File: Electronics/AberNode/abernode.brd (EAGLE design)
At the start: 100 x 80 mm, 12 parts, among them IC1 MCP1703CB, Y1 16MHZ, Y2 16MHZ

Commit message: Schematic Mostly Done
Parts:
- removed Y1: 16MHZ, SparkFun-FreqCtrl:RESONATOR-SMD
- added BATT, SOLAR: M02LOCK, SparkFun-Connectors:1X02_LOCK
- added C6, C9: 10uF, resistor:C0805
- added C7: (no value), resistor:E7,5-18
- added CHRG/LBO: ORANGE, led:CHIPLED_0603
- added CON4: (no value), SparkFun-Connectors:1X06_LONGPADS
- added D1: MBR0520LT, diode:SOD123
- added DONE: GREEN, led:CHIPLED_0603
- added IC2: MCP73871, adafruit:QFN20
- added PWR: RED, led:CHIPLED_0603
- added R2, R3, R9: 10k, resistor:R0805
- added R4: 2K, resistor:R0805
- added R5: 100K, resistor:R0805
- added R6, R7, R8: 1K, resistor:R0805
- added U$1: (no value), tom:ANT
- added U$2, U$3, U$4: HEADER_4, tom:HEADER_4
- moved R1 96.7 mm to (35.8, 40.8), turned to 90 degrees
- moved C5 94.8 mm to (32.3, 36.3)
- moved Y2 89.4 mm to (31.5, 43.9), turned to 90 degrees
- moved FLASH 82.5 mm to (36.0, 57.7)
- moved C4 74.9 mm to (11.0, 41.4), turned to 180 degrees
- moved C2 71.6 mm to (27.3, 29.5)
- moved C1 70.8 mm to (31.8, 24.5)
- moved RFM 63.7 mm to (22.0, 52.8), flipped to the bottom, turned to 90 degrees
- moved C3 63.0 mm to (32.0, 27.1)
- moved IC1 56.2 mm to (31.8, 30.5), turned to 270 degrees
- moved ATMEGA 50.3 mm to (21.9, 42.2), turned to 180 degrees
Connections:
- removed net PSBATT: C1.2, C3.2, IC1.3
- removed net VCC: C2.2, IC1.2
- new net ANALOG_1: ATMEGA.37, U$2.4
- new net ANALOG_2: ATMEGA.36, U$3.4
- new net ANALOG_3: ATMEGA.35, U$4.4
- new net ANALOG_4: ATMEGA.34, CON4.6
- new net DIGIT_1: ATMEGA.9, U$2.3
- new net DIGIT_2: ATMEGA.10, U$3.3
- new net DIGIT_3: ATMEGA.11, U$4.3
- new net N$10: CHRG/LBO.A, R8.1
- new net N$11: IC2.6, PWR.C
- new net N$12: DONE.C, IC2.7
- new net N$13: CHRG/LBO.C, IC2.8
- new net N$14: D1.A, SOLAR.2
- new net N$17: IC2.5, R9.2
- new net N$5: IC2.12, R5.2
- new net N$6: IC2.2, R2.2, R3.1
- new net N$7: IC2.13, R4.2
- new net N$8: PWR.A, R6.1
- new net N$9: DONE.A, R7.1
- new net SCL: ATMEGA.19, CON4.5
- new net SDA: ATMEGA.20, CON4.4
- new net VBATT: BATT.2, C6.2, IC2.14, IC2.15, IC2.16
- new net VIN: C7.+, C9.2, CON4.2, D1.C, IC2.17, IC2.18, IC2.19, IC2.3, IC2.4, IC2.9, R3.2, R6.2, R7.2, R8.2
- new net VSUPPLY: C1.2, C3.2, IC1.3, IC2.1, IC2.20
- net +3V3: now also C2.2, CON4.1, IC1.2, U$2.2, U$3.2, U$4.2
- net ANT: now also U$1.P$1
- net GND: now also BATT.1, C6.1, C7.-, C9.1, CON4.3, IC2.10, IC2.11, R2.1, R4.1, R5.1, R9.1, SOLAR.1, U$2.1, U$3.1, U$4.1
- net N$3: now also ATMEGA.29
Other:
- board size 100 x 80 mm -> 40.6 x 65.9 mm

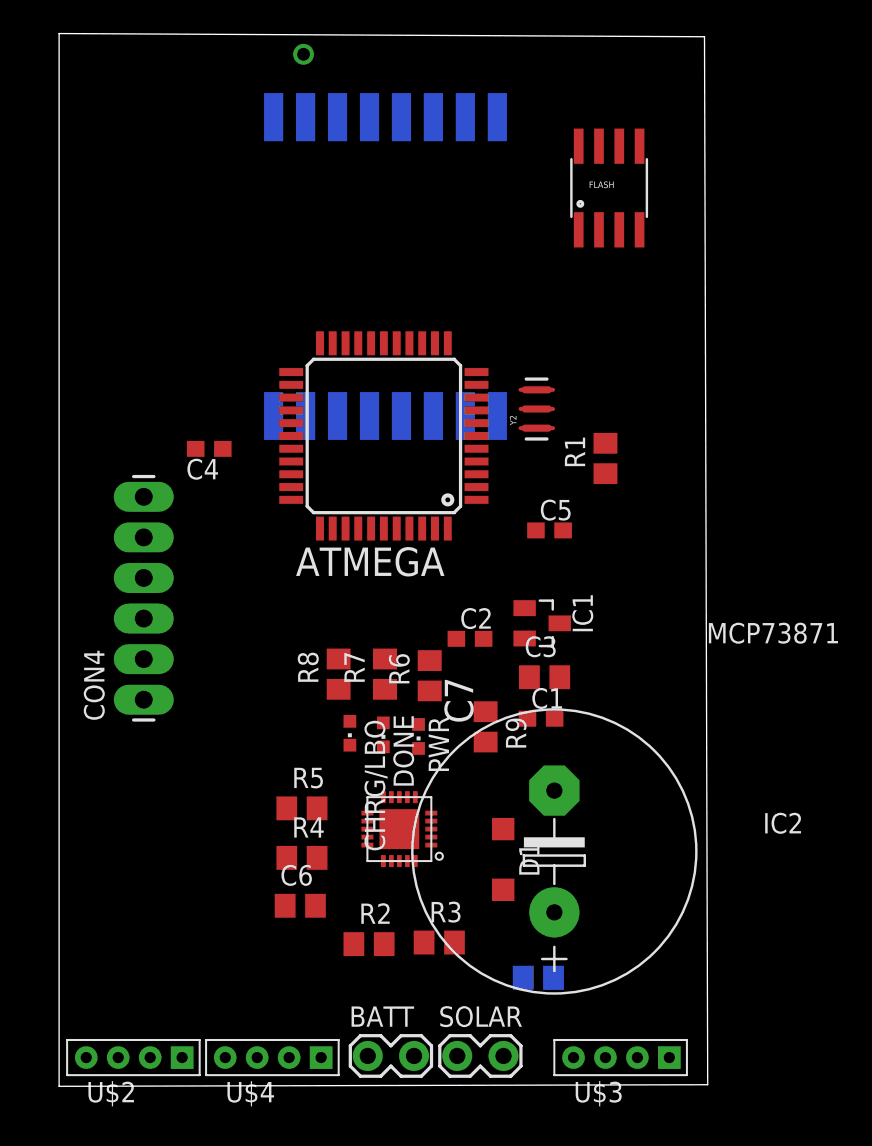
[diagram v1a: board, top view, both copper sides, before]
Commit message: Board Designed minus res values
Need to sort out the resistor values for the mcp73871 pullups battery
sense and charging rates.
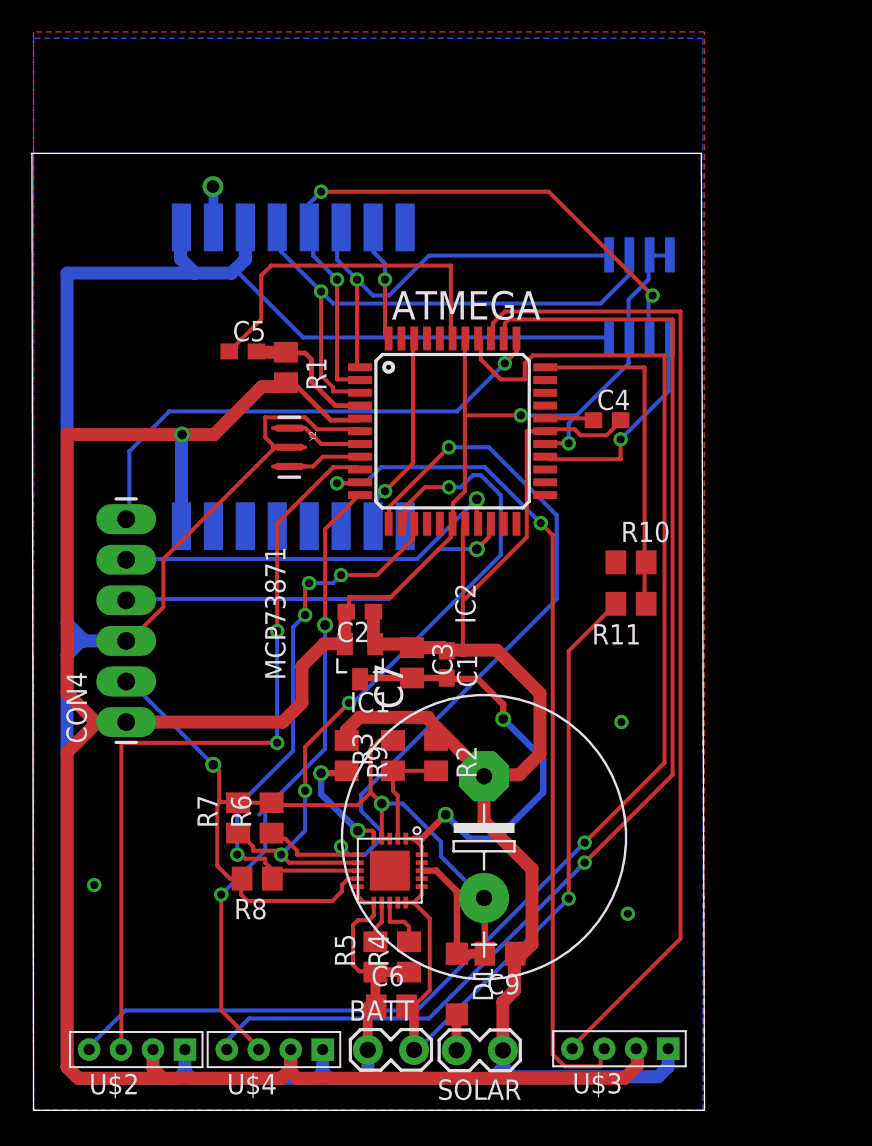
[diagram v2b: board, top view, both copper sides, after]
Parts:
- removed CHRG/LBO: ORANGE, led:CHIPLED_0603
- removed DONE: GREEN, led:CHIPLED_0603
- removed PWR: RED, led:CHIPLED_0603
- added R10, R11: 10k, resistor:R0805
- moved C4 25.0 mm to (35.9, 43.2), turned to 0 degrees
- moved C5 22.2 mm to (13.1, 47.5)
- moved R1 20.8 mm to (15.8, 46.5), turned to 270 degrees
- moved Y2 15.7 mm to (16.0, 41.5), turned to 270 degrees
- moved R8 13.8 mm to (14.0, 14.5), turned to 180 degrees
- moved R6 13.3 mm to (14.9, 18.3)
- moved R7 12.9 mm to (12.8, 18.3)
- moved R2 12.5 mm to (25.2, 22.2), turned to 270 degrees
- moved R3 12.1 mm to (22.5, 22.2), turned to 90 degrees
- moved IC1 11.6 mm to (20.4, 28.1), turned to 180 degrees
- moved R5 10.4 mm to (21.4, 9.60), turned to 90 degrees
- moved U$1 10.0 mm to (11.2, 57.8), flipped to the bottom
- moved R4 9.13 mm to (23.5, 9.60), turned to 90 degrees
- moved RFM 8.99 mm to (16.3, 45.9)
- moved R9 8.88 mm to (19.6, 22.2)
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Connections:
- removed net N$10: CHRG/LBO.A, R8.1
- removed net N$11: IC2.6, PWR.C
- removed net N$12: DONE.C, IC2.7
- removed net N$13: CHRG/LBO.C, IC2.8
- removed net N$8: PWR.A, R6.1
- removed net N$9: DONE.A, R7.1
- new net BATT_SENSE: ATMEGA.33, R10.2, R11.1
- new net PG: ATMEGA.12, IC2.6, R6.1
- new net STAT1: ATMEGA.14, IC2.8, R8.1
- new net STAT2: ATMEGA.13, IC2.7, R7.1
- net GND: now also R10.1
- net VBATT: now also R11.2
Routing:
- net GND: track 0.00 -> 294.8 mm, vias 0 -> 3
- net +3V3: track 0.00 -> 176.8 mm, vias 0 -> 3
- net ANALOG_1: track 0.00 -> 83.7 mm, vias 0 -> 1
- net ANALOG_3: track 0.00 -> 75.4 mm, vias 0 -> 1
- net VIN: track 0.00 -> 65.9 mm, vias 0 -> 2
- net ANALOG_2: track 0.00 -> 62.0 mm
- net DIGIT_2: track 0.00 -> 54.2 mm, vias 0 -> 2
- net PG: track 0.00 -> 50.6 mm, vias 0 -> 2
- net DIGIT_1: track 0.00 -> 49.4 mm, vias 0 -> 2
- net VBATT: track 0.00 -> 46.5 mm, vias 0 -> 1
- net STAT2: track 0.00 -> 45.3 mm, vias 0 -> 4
- net MISO: track 0.00 -> 40.6 mm, vias 0 -> 3
- net DIGIT_3: track 0.00 -> 39.9 mm, vias 0 -> 2
- net STAT1: track 0.00 -> 36.6 mm, vias 0 -> 4
- net SCK: track 0.00 -> 35.1 mm, vias 0 -> 1
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- added copper zone on layer 1, net GND
- added copper zone on layer 16, net GND
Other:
- board size 40.6 x 65.9 mm -> 42.1 x 59.9 mm

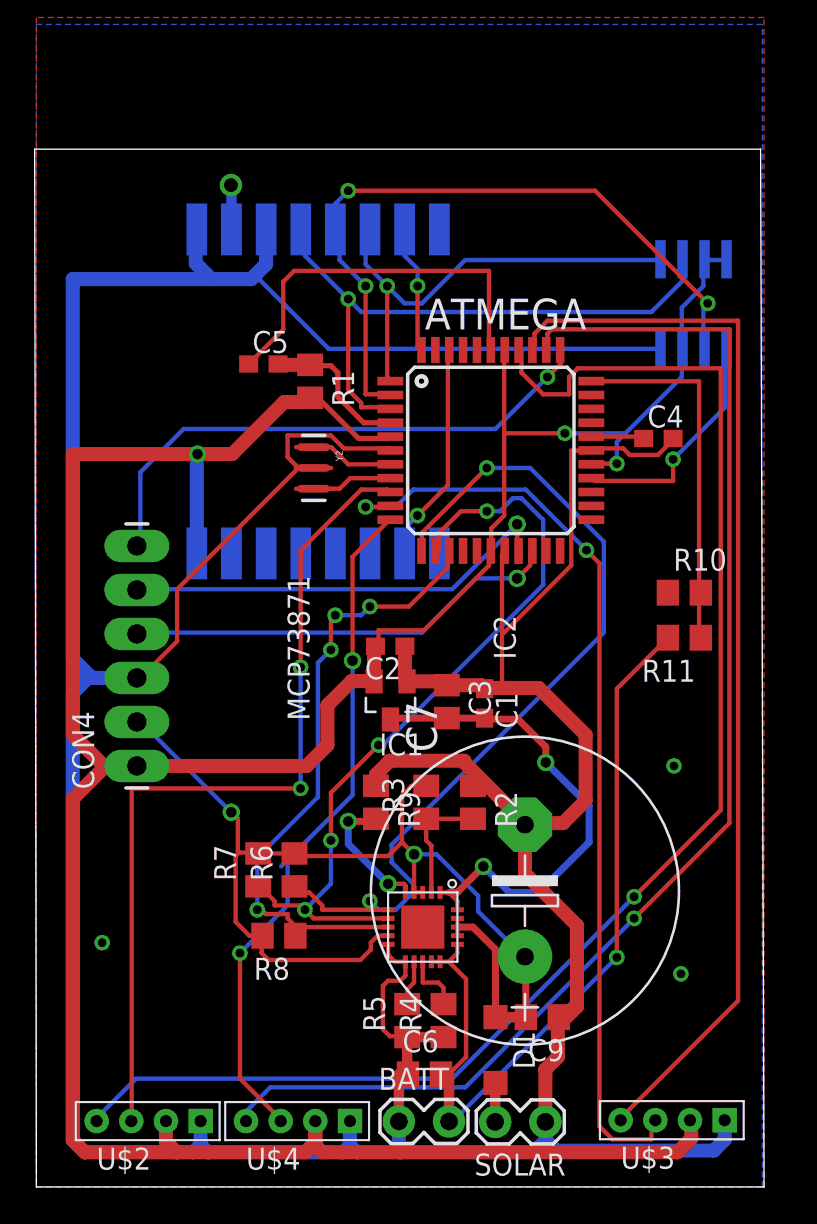
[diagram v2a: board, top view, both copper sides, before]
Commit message: Board redesign
Moved components around, changed orientation of connectors. Added extra
sensor connector. Power to bottom sensor connectors is driven from a
iopin to reduce current draw whilst sleeping.
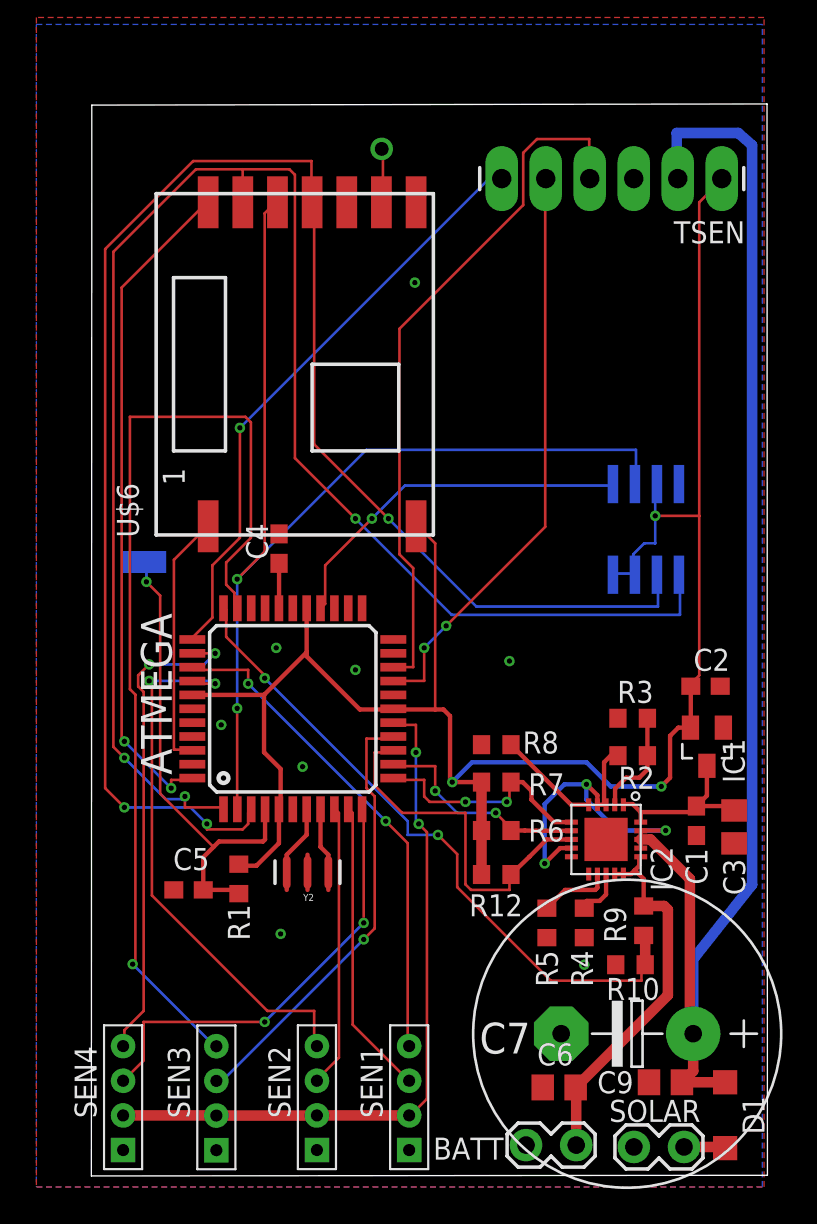
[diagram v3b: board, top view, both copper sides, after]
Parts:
- removed CON4: (no value), SparkFun-Connectors:1X06_LONGPADS
- removed R11: 10k, resistor:R0805
- removed RFM: RFM69HW, SparkFun-RF:RFM69W-XXXS2
- removed U$1: (no value), tom:ANT
- removed U$2, U$3, U$4: HEADER_4, tom:HEADER_4
- added R12: 10K, resistor:R0603
- added RST: (no value), wirepad:SMD1,27-2,54
- added SEN1, SEN2, SEN3, SEN4: HEADER_4, tom:HEADER_4
- added TSEN: (no value), SparkFun-Connectors:1X06_LONGPADS
- added U$6: RFM69HW, tom:RFM69W-XXXS2
- added U$7: (no value), tom:ANT
- C7: value (none) -> 4700u
- R1, R2, R3: value 10k -> 10K; device resistor:R0805 -> resistor:R0603
- R10, R9: value 10k -> 1M; device resistor:R0805 -> resistor:R0603
- R4: value 2K -> 4K; device resistor:R0805 -> resistor:R0603
- R5: device resistor:R0805 -> resistor:R0603
- R6, R7, R8: value 1K -> 10K; device resistor:R0805 -> resistor:R0603
- moved C5 30.7 mm to (8.78, 17.1)
- moved R1 29.0 mm to (11.7, 17.8), turned to 90 degrees
- moved Y2 23.3 mm to (15.7, 18.2), turned to 0 degrees
- moved C4 22.8 mm to (14.0, 36.8), turned to 90 degrees
- moved R10 21.7 mm to (34.3, 12.8)
- moved ATMEGA 18.8 mm to (14.8, 27.6), turned to 90 degrees
- moved IC1 18.5 mm to (38.7, 25.4)
- moved C2 18.3 mm to (38.6, 28.9)
- moved C3 18.1 mm to (40.3, 20.8), turned to 90 degrees
- moved R9 16.9 mm to (35.1, 15.4), turned to 90 degrees
- moved R8 16.7 mm to (26.5, 25.5), turned to 0 degrees
- moved R7 14.6 mm to (26.5, 23.4), turned to 180 degrees
- moved C1 14.0 mm to (38.1, 21.1), turned to 90 degrees
- moved D1 13.8 mm to (39.8, 4.14)
- moved FLASH 13.3 mm to (35.2, 38.0), turned to 180 degrees
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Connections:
- removed net ANT: RFM.10, U$1.P$1
- removed net N$4: ATMEGA.4, C5.2, R1.1
- new net ANALOG_5: ATMEGA.32, SEN3.4
- new net DIGIT_5: ATMEGA.15, SEN3.3
- new net N$12: U$6.ANT, U$7.P$1
- new net RESET: ATMEGA.4, C5.2, R1.1, RST.1
- new net SENSE_PWR: ATMEGA.16, SEN1.2, SEN2.2, SEN3.2, SEN4.2
- net +3V3: now also R12.2, R6.2, R7.2, TSEN.1, U$6.3V3; no longer CON4.1, RFM.8, U$2.2, U$3.2, U$4.2
- net ANALOG_1: now also SEN2.4; no longer U$2.4
- net ANALOG_2: now also SEN1.4; no longer U$3.4
- net ANALOG_3: now also SEN4.4; no longer U$4.4
- net ANALOG_4: now also TSEN.6; no longer CON4.6
- net BATT_SENSE: now also R9.1; no longer R11.1
- net DIGIT_1: now also SEN2.3; no longer U$2.3
- net DIGIT_2: now also SEN1.3; no longer U$3.3
- net DIGIT_3: now also SEN4.3; no longer U$4.3
- net GND: now also R3.1, R8.1, SEN1.1, SEN2.1, SEN3.1, SEN4.1, TSEN.3, U$6.GND, U$6.GND$1; no longer CON4.3, R2.1, R9.1, RFM.11, RFM.9, U$2.1, U$3.1, U$4.1
- net INT_RFM: now also U$6.DI0; no longer RFM.2
- net MISO: now also U$6.MISO; no longer RFM.13
- net MOSI: now also U$6.MOSI; no longer RFM.14
- net N$17: now also R8.2; no longer R9.2
- net N$6: now also R2.1, R3.2; no longer R2.2, R3.1
- net PG: now also R7.1; no longer R6.1
- net SCK: now also U$6.SCK; no longer RFM.12
- net SCL: now also TSEN.5; no longer CON4.5
- net SDA: now also TSEN.4; no longer CON4.4
- net SS_RFM: now also U$6.SS; no longer RFM.15
- net STAT1: now also R12.1; no longer R8.1
- net STAT2: now also R6.1; no longer R7.1
- net VBATT: now also R9.2; no longer R11.2
- net VIN: now also R2.2, TSEN.2; no longer CON4.2, R3.2, R6.2, R7.2, R8.2
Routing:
- net GND: track 294.8 -> 0.00 mm, vias 3 -> 8
- net MOSI: track 26.7 -> 96.1 mm, vias 1 -> 3
- net +3V3: track 176.8 -> 114.0 mm
- net SCK: track 35.1 -> 97.7 mm, vias 1 -> 3
- net ANALOG_5: track 0.00 -> 57.3 mm, vias 0 -> 1
- net ANALOG_1: track 83.7 -> 32.0 mm, vias 1 -> 2
- net ANALOG_3: track 75.4 -> 28.3 mm, vias 1 -> 2
- net SENSE_PWR: track 0.00 -> 41.3 mm, vias 0 -> 2
- net DIGIT_2: track 54.2 -> 17.2 mm, vias 2 -> 0
- net PG: track 50.6 -> 13.7 mm
- net VIN: track 65.9 -> 100.4 mm, vias 2 -> 3
- net ANALOG_2: track 62.0 -> 28.9 mm, vias 0 -> 2
- net DIGIT_1: track 49.4 -> 16.3 mm, vias 2 -> 0
- net STAT2: track 45.3 -> 12.8 mm, vias 4 -> 2
- net SS_RFM: track 7.38 -> 38.8 mm, vias 1 -> 2
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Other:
- board size 42.1 x 59.9 mm -> 39 x 61.9 mm

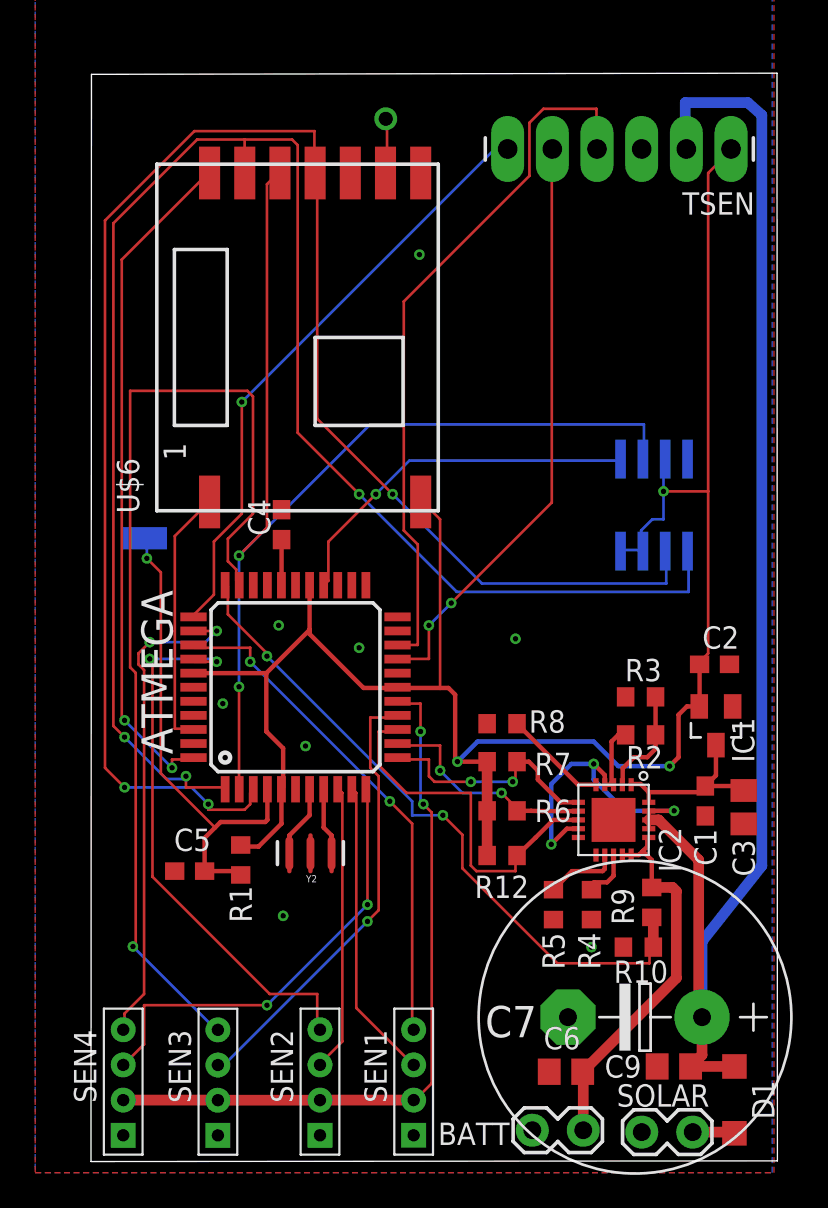
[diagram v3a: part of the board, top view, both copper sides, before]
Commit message: Mostly Done
Routed power to connectors through io pin, added reset pad for
programming.
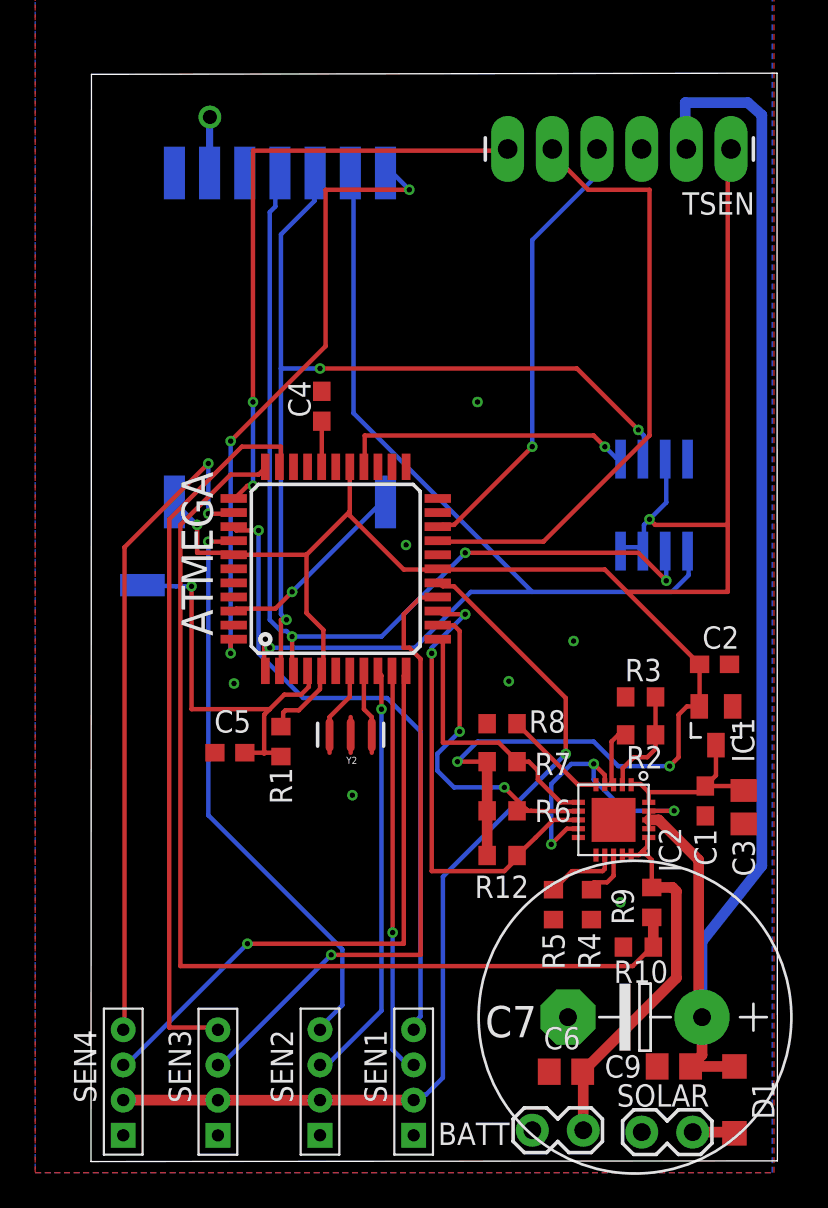
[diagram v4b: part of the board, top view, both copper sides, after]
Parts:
- moved U$7 10.0 mm to (9.93, 60.0)
- moved ATMEGA 7.11 mm to (17.1, 34.3)
- moved C5 7.11 mm to (11.1, 23.9)
- moved Y2 7.11 mm to (17.9, 24.9)
- moved R1 7.11 mm to (14.0, 24.5)
- moved C4 7.11 mm to (16.3, 43.6)
- moved RST 2.67 mm to (6.10, 33.4)
- flipped U$6 to the bottom
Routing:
- net SCK: track 97.7 -> 55.1 mm
- net MOSI: track 96.1 -> 56.8 mm, vias 3 -> 1
- net BATT_SENSE: track 38.4 -> 60.3 mm, vias 2 -> 0
- net ANALOG_5: track 57.3 -> 40.9 mm, vias 1 -> 0
- net SDA: track 40.6 -> 25.7 mm, vias 0 -> 1
- net SENSE_PWR: track 41.3 -> 53.3 mm, vias 2 -> 1
- net MISO: track 64.2 -> 53.2 mm, vias 2 -> 3
- net DIGIT_5: track 25.5 -> 36.5 mm
- net ANALOG_3: track 28.3 -> 38.5 mm
- net DIGIT_3: track 25.6 -> 34.4 mm, vias 2 -> 1
- net ANALOG_2: track 28.9 -> 36.9 mm, vias 2 -> 1
- net DIGIT_1: track 16.3 -> 24.3 mm, vias 0 -> 1
- net +3V3: track 114.0 -> 121.5 mm, vias 3 -> 4
- net STAT2: track 12.8 -> 19.4 mm
- net DIGIT_2: track 17.2 -> 23.2 mm, vias 0 -> 1
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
